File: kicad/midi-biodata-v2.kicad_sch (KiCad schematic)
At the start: 39 parts, among them J1 DIN-5_180degree, J2 PJ-320B, J3 Conn_01x14_Pin, J4 PJ-320B, J5 PJ-320B, J6 PJ-320B, J7 Conn_01x02_Socket, J8 DIN-5_180degree, U1 SN74LVC1G07DBVR, U2 TLP2362TPR_E, U3 LMC555xM, U4 ESP32-S3_SUPERMINI_TH

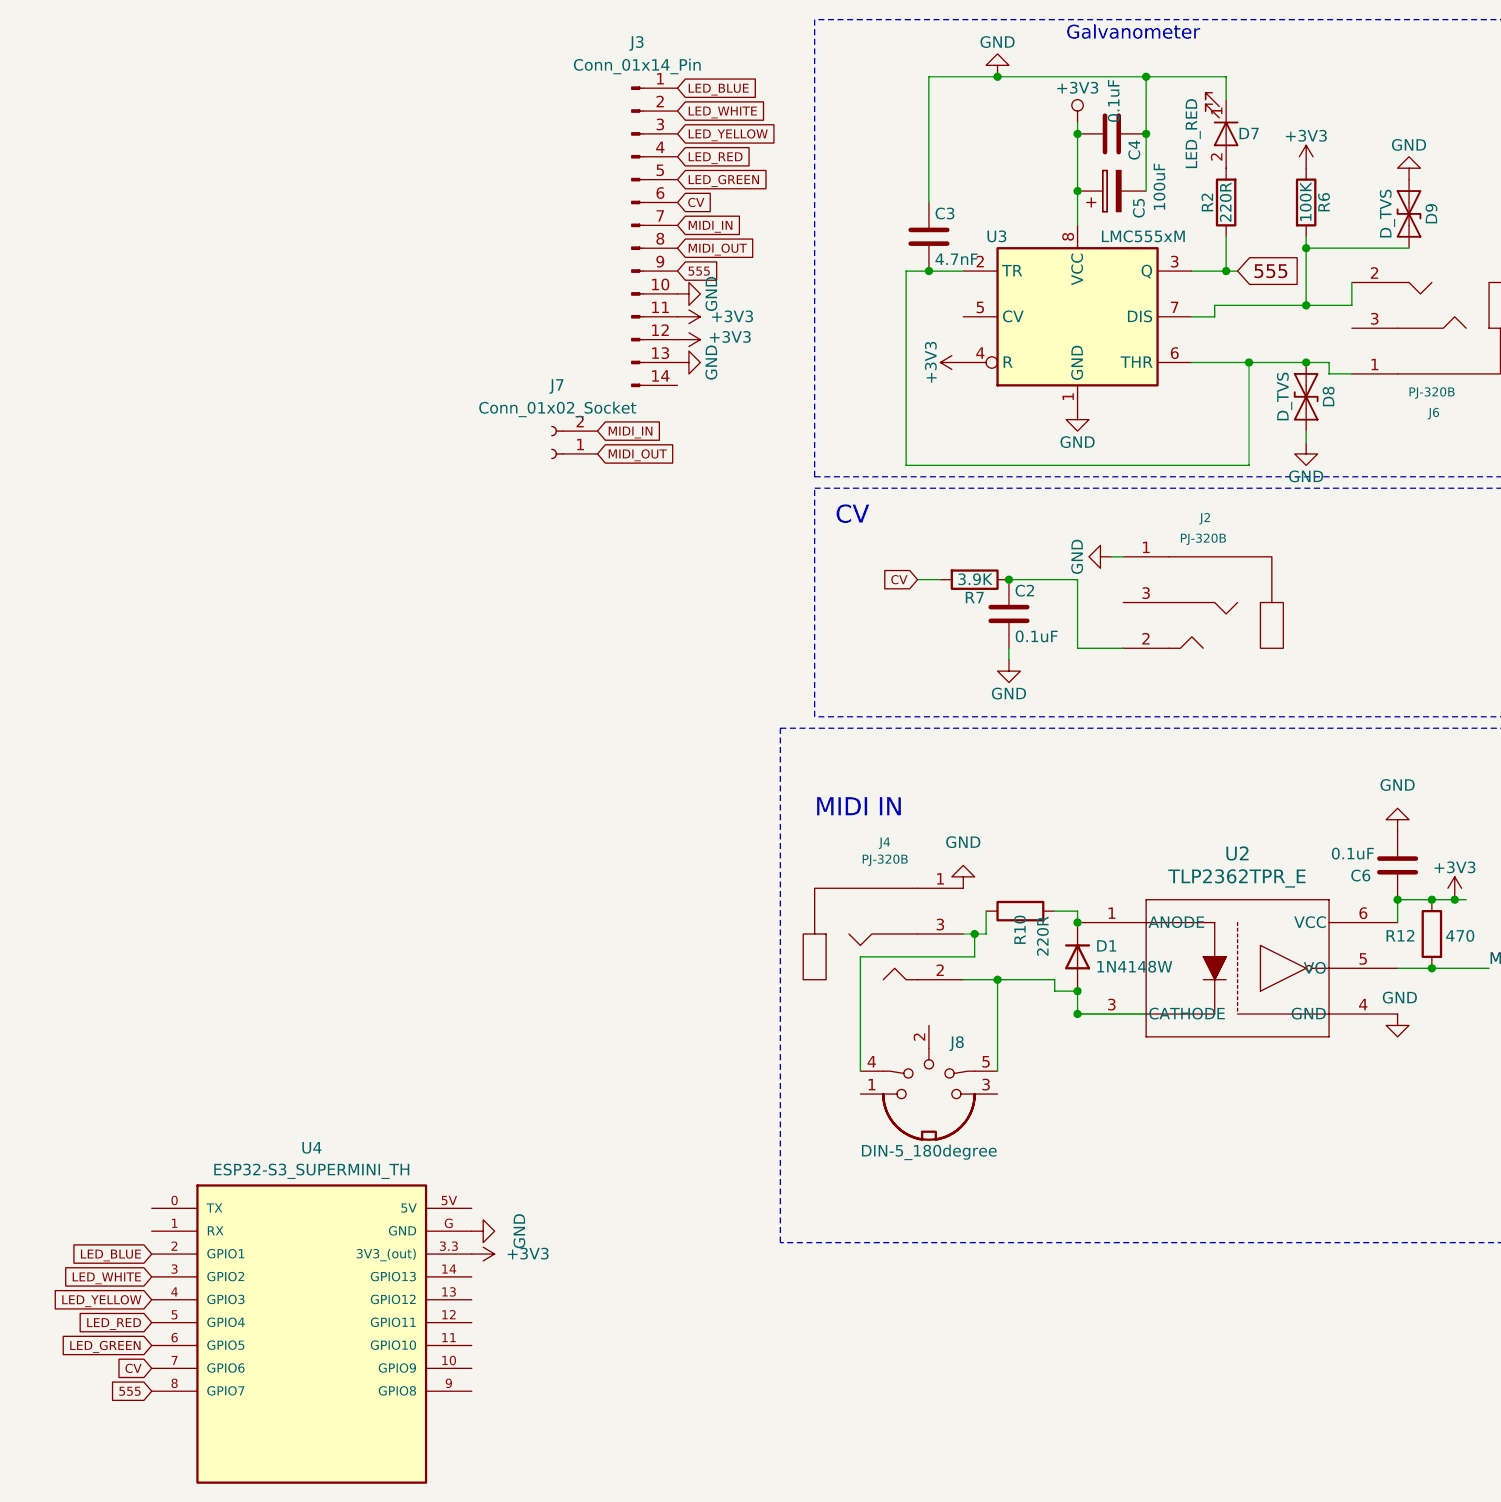
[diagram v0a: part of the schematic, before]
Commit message: update board to 0.3, add analog partition to board
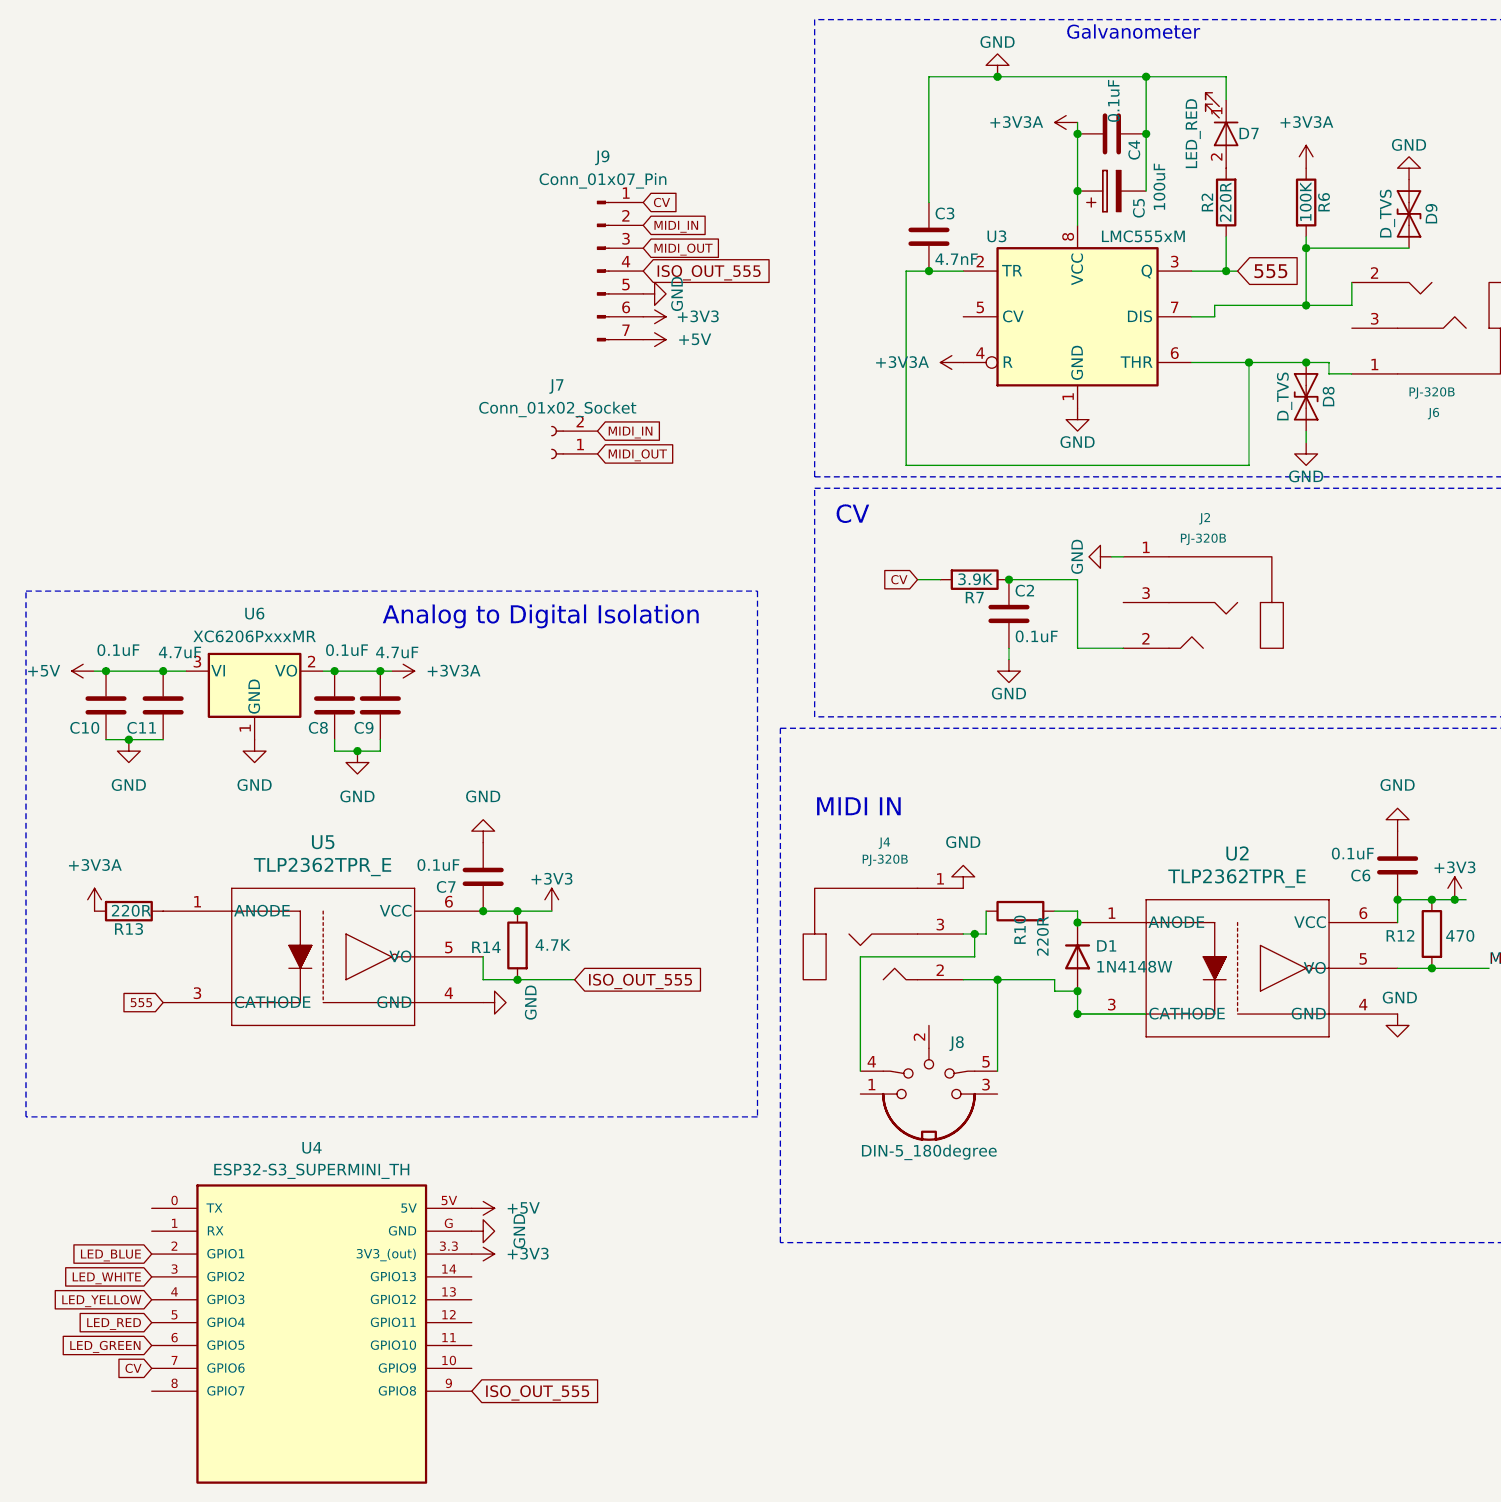
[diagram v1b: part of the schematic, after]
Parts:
- removed J3: Conn_01x14_Pin, Connector_PinHeader_2.54mm:PinHeader_1x13_P2.54mm_Vertical, symbol Connector:Conn_01x14_Pin
- added C10, C8: 0.1uF, Capacitor_SMD:C_0402_1005Metric, symbol midi-biodata-v2-rescue:C
- added C11, C9: 4.7uF, Capacitor_SMD:C_0402_1005Metric, symbol midi-biodata-v2-rescue:C
- added C7: 0.1uF, Capacitor_SMD:C_0402_1005Metric, symbol Device:C
- added J9: Conn_01x07_Pin, Connector_PinHeader_2.54mm:PinHeader_1x07_P2.54mm_Vertical, symbol Connector:Conn_01x07_Pin
- added R13: 220R, Resistor_SMD:R_0402_1005Metric, symbol midi-biodata-v2-rescue:R
- added R14: 4.7K, Resistor_SMD:R_0805_2012Metric, symbol Device:R
- added U5: TLP2362TPR_E, poma:tlp2362, symbol Sleep-lib:TLP2362TPR_E
- added U6: XC6206PxxxMR, Package_TO_SOT_SMD:SOT-23-3, symbol Regulator_Linear:XC6206PxxxMR
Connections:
- net +3V3: now also C7.1, J9.6 (Pin_6), R14.1, U5.6 (VCC); no longer C4.2, C5.1, R6.1, U3.4 (R), U3.8 (VCC)
- net 555: now also U5.3 (CATHODE); no longer U4.8 (GPIO7)
- net CV: now also J9.1 (Pin_1)
- net GND: now also C10.1, C11.1, C7.2, C8.1, C9.1, J9.5 (Pin_5), U5.4 (GND), U6.1 (GND)
- net MIDI_IN: now also J9.2 (Pin_2)
- net MIDI_OUT: now also J9.3 (Pin_3)
- net +5V: now reaches U4.5V
- net +5V: now also C10.2, C11.2, J9.7 (Pin_7), U6.3 (VI)
- net ISO_OUT_555: now reaches U4.9 (GPIO8)
- net ISO_OUT_555: now also J9.4 (Pin_4), R14.2, U5.5 (VO)
- new net: R13.1, U5.1 (ANODE)
- new net +3V3A: C4.2, C5.1, C8.2, C9.2, R13.2, R6.1, U3.4 (R), U3.8 (VCC), U6.2 (VO)
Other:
- note added: "Analog to Digital Isolation"
- company: 13-37.org electronics -> Hanz Tech Inc
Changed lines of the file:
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@@
 	(title_block
 		(title "MIDI Biodata Sonification Device ")
-		(date "2018-01-12")
+		(date "2025-08-01")
 		(rev "0.3")
-		(company "13-37.org electronics")
+		(company "Hanz Tech Inc")
 	)
